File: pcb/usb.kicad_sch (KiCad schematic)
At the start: 22 parts, among them J8 USB-A_USB-303WSD-BRY, J9 USB-C_TYPE-C_16PLT-H6.5, U8 AP22615AWU-7

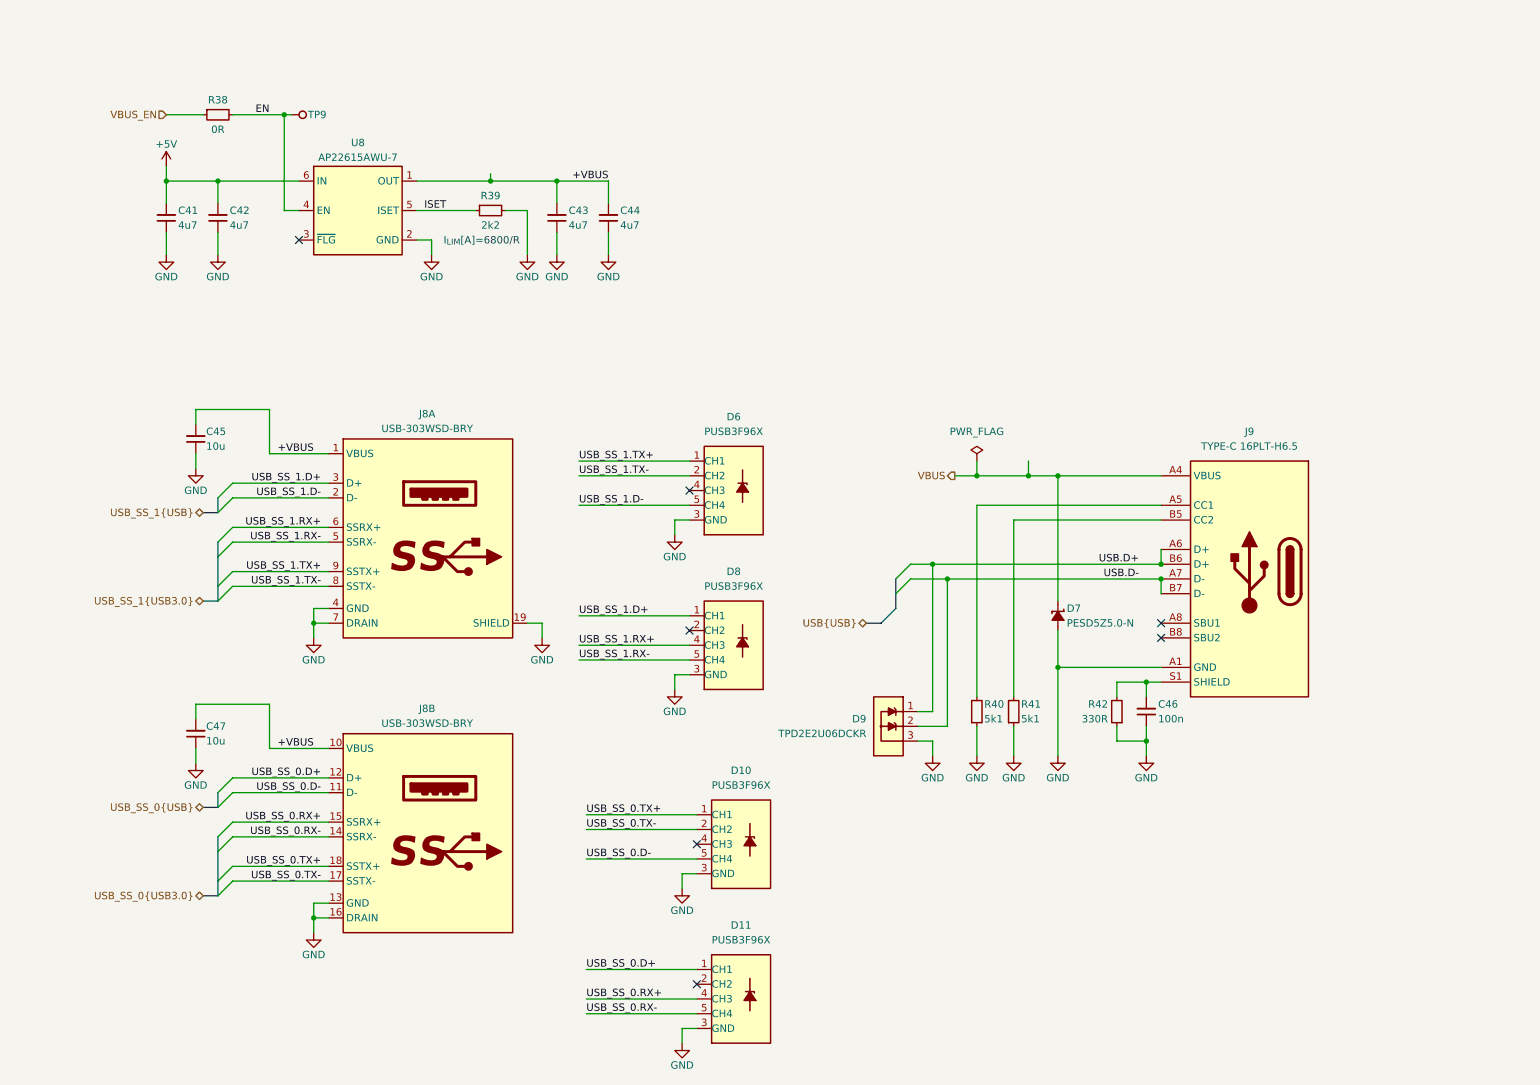
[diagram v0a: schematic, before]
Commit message: [#5] Refactor the schematic
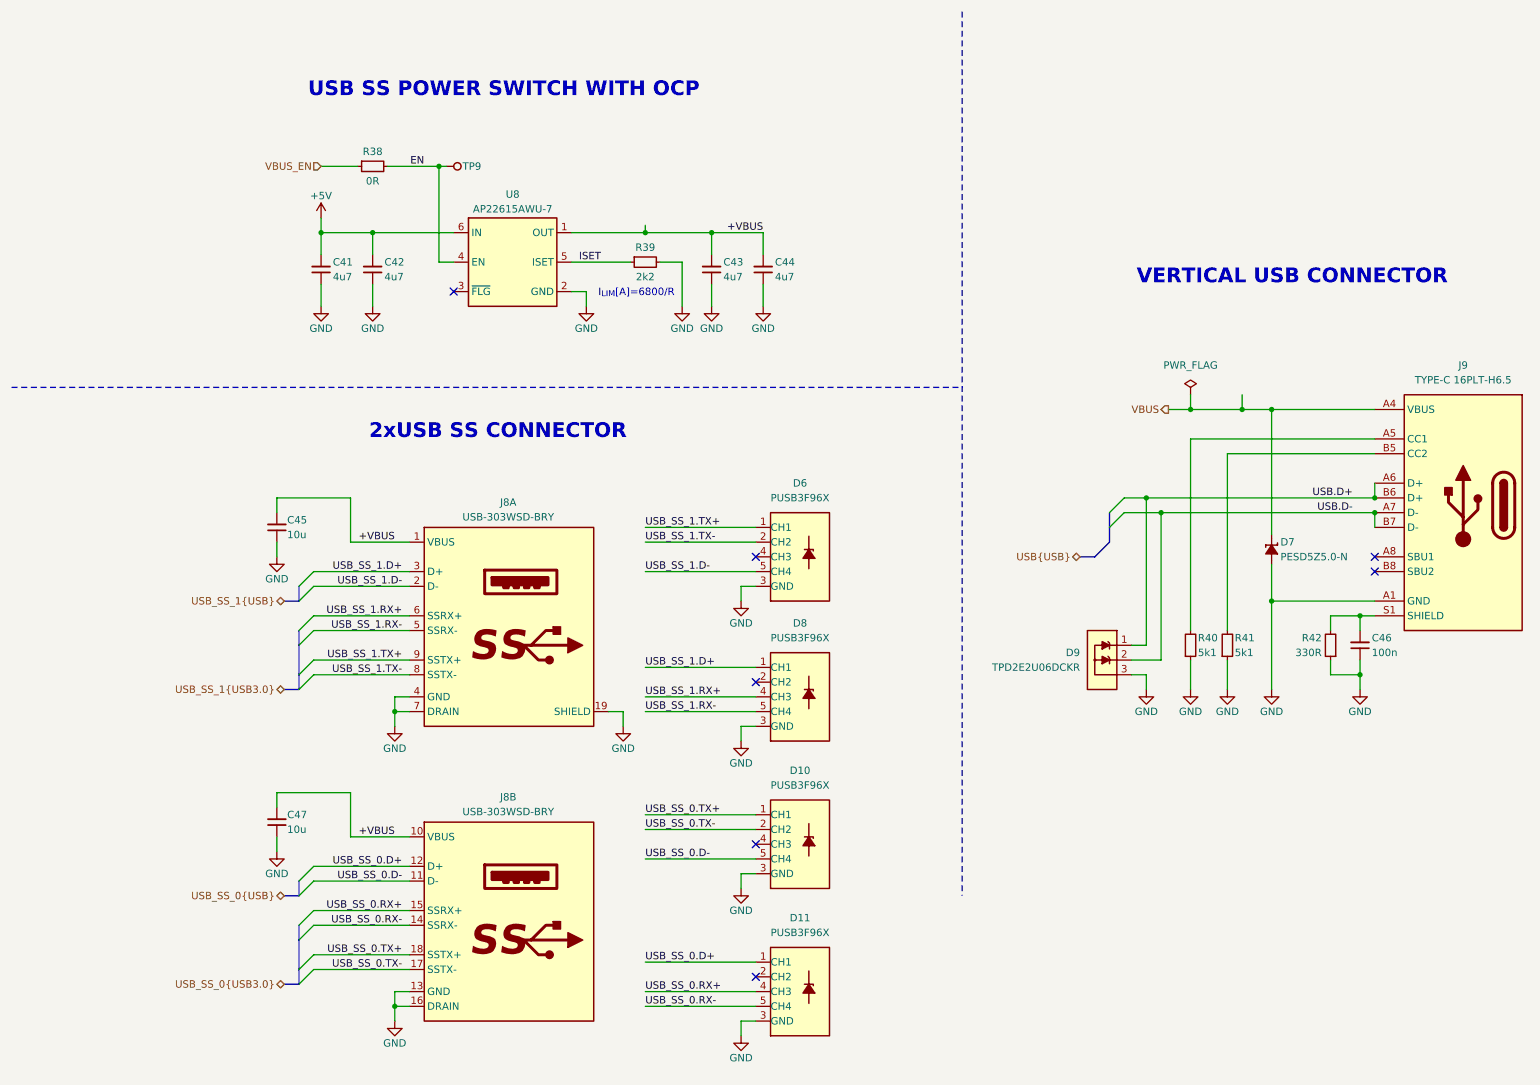
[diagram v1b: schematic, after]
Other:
- note added: "2xUSB SS CONNECTOR"
- note added: "USB SS POWER SWITCH WITH OCP"
- note added: "VERTICAL USB CONNECTOR"
- moved on the sheet: C41, C42, C43, C44, C45, C46, C47, D10, D11, D6, D7, D8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
